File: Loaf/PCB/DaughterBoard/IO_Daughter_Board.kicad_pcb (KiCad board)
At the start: 2 copper layers, 93 x 90.5 mm, 12 parts, among them J1 I/O Block, J2 5V Block, J3 DB25_Socket, J4 Ground Block, J5 Ground Block, J6 Barrel Jack, SW1 SW_Push_Open, SW2 SW_Push_Open

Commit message: Update IO_Daughter_Board.kicad_pcb
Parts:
- SW1: value SW_Push_Open -> ESTOP
- SW2: value SW_Push_Open -> RESET
- moved J2 54.6 mm to (144.5, 67.0), turned to 180 degrees
- moved R2 34.9 mm to (172.6, 79.6)
- moved R3 34.9 mm to (163.1, 79.6)
- moved SW1 34.9 mm to (175.6, 85.8)
- moved SW2 34.9 mm to (159.3, 85.8)
- moved VRM1 14.3 mm to (153.6, 105.6), turned to 180 degrees
- moved J4 2.81 mm to (186.7, 67.0), turned to 180 degrees
- moved J1 0.28 mm to (104.2, 72.7)
- moved J5 0.25 mm to (188.8, 110.8)
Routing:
- net +3.3V: track 0.00 -> 23.8 mm
- net /ESTOP: track 49.6 -> 63.9 mm, vias 0 -> 2
- net /RESET: track 52.3 -> 65.1 mm, vias 0 -> 2
- net +12V: track 21.8 -> 21.1 mm
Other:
- board size 93 x 90.5 mm -> 93 x 55.7 mm

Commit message: Updated Daughter Board
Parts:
- removed R2: 10K, Resistor_THT:R_Axial_DIN0204_L3.6mm_D1.6mm_P7.62mm_Horizontal
- removed SW2: RESET, Button_Switch_THT:SW_PUSH_1P1T_6x3.5mm_H5.0_APEM_MJTP1250
- added J7: Screw_Terminal_01x02, Connector_AMASS:AMASS_XT30UPB-M_1x02_P5.0mm_Vertical, F.Cu at (170.4, 77.7)
- added Logo1: Logo_Open_Hardware_Small, Symbol:OSHW-Symbol_6.7x6mm_SilkScreen, F.Cu at (134.5, 73.8)
- SW1: value ESTOP -> SW_Push; footprint Button_Switch_THT:SW_PUSH_1P1T_6x3.5mm_H5.0_APEM_MJTP1250 -> Button_Switch_THT:SW_Tactile_Straight_KSL0Axx1LFTR
- moved SW1 54.3 mm to (121.3, 86.9)
- moved R3 28.4 mm to (143.4, 100.1)
- moved VRM1 27.6 mm to (179.3, 95.7), turned to -90 degrees
- moved J2 8.74 mm to (174.7, 100.3)
- moved C4 7.63 mm to (137.9, 99.7)
- moved J1 7.47 mm to (156.1, 104.7)
- moved J6 4.08 mm to (184.8, 110.9)
- moved J3 4.01 mm to (108.2, 72.9)
- renumbered J3 to J1, J6 to J2, J1 to J3, J2 to J4, J4 to J5, J5 to J6
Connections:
- C4 pad 1: +5V -> +5V Slice
- J1 pad 20: +5V -> +5V Slice
- J1 pad 7: +5V -> +5V Slice
- J2 pad 1: GND -> +12V
- J2 pad 2: +12V -> GND
- SW1 pad 2: /ESTOP -> /RESET
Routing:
- net +5V: track 0.00 -> 178.9 mm, vias 0 -> 11
- net /RESET: track 65.1 -> 84.2 mm
- net /ESTOP: track 63.9 -> 48.8 mm
- net GND: track 13.5 -> 0.00 mm
- net +5V Slice: track 0.00 -> 8.43 mm
- net /DIO2: track 78.3 -> 71.9 mm
- net /DIO4: track 70.2 -> 64.0 mm
- net /DIO5: track 69.1 -> 62.9 mm
- net /DIO6: track 62.4 -> 56.2 mm
- net /AIO0: track 32.3 -> 26.1 mm
- net /DIO7: track 61.1 -> 55.1 mm
- net /AIO3: track 31.5 -> 25.5 mm
- net /DIO0: track 85.7 -> 79.7 mm
- net /DIO1: track 84.6 -> 78.6 mm
- net /AIO6: track 24.9 -> 30.8 mm
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- added copper zone on F.Cu, net GND
- removed copper zone on F.Cu, net +5V
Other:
- board size 93 x 55.7 mm -> 84.5 x 50.1 mm
- board text added: "Analog I/O"
- board text added: "BREAD I/O Board V1 oshe.io REV 2026"
- board text added: "Digital I/O"
- board text added: "EMERGENCY STOP"
- board text added: "RESET"

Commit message: See Description
Rebuilt I/O Slice daughter board.
Added transmission to the Input slice.
Got digital reading working on input slice.
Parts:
- added H1: MountingHole_Pad, MountingHole:MountingHole_3.2mm_M3_DIN965_Pad, F.Cu at (86.0, 123.0)
- added H2: MountingHole_Pad, MountingHole:MountingHole_3.2mm_M3_DIN965_Pad, F.Cu at (178.0, 123.0)
- added H3: MountingHole_Pad, MountingHole:MountingHole_3.2mm_M3_DIN965_Pad, F.Cu at (93.0, 88.0)
- added H4: MountingHole_Pad, MountingHole:MountingHole_3.2mm_M3_DIN965_Pad, F.Cu at (171.0, 88.0)
- added H5: MountingHole_Pad, MountingHole:MountingHole_3.2mm_M3_DIN965_Pad, F.Cu at (141.5, 103.1)
- added J8: Conn_01x02_Pin, Connector_PinHeader_2.54mm:PinHeader_1x02_P2.54mm_Horizontal, F.Cu at (172.8, 116.5)
- J7: footprint Connector_AMASS:AMASS_XT30UPB-M_1x02_P5.0mm_Vertical -> TerminalBlock:TerminalBlock_MaiXu_MX126-5.0-02P_1x02_P5.00mm
- moved J6 103.9 mm to (85.9, 79.0), turned to -90 degrees
- moved J4 60.4 mm to (178.2, 117.1), turned to 90 degrees
- moved J7 50.4 mm to (147.4, 122.6), turned to 0 degrees
- moved Logo1 35.6 mm to (106.3, 95.5)
- moved C4 29.7 mm to (111.4, 113.0), turned to 90 degrees
- moved SW1 28.5 mm to (114.2, 114.5), turned to 90 degrees
- moved J1 26.9 mm to (133.3, 119.1)
- moved R3 23.1 mm to (120.5, 103.3), turned to 180 degrees
- moved J3 22.8 mm to (129.7, 80.7), turned to 180 degrees
- moved J5 19.7 mm to (172.6, 80.7)
- moved J2 19.3 mm to (161.7, 114.6)
- moved VRM1 18.7 mm to (170.2, 112.0), turned to 180 degrees
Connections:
- J3 pad 10: /AIO1 -> /AIO6
- J3 pad 11: /AIO2 -> /AIO5
- J3 pad 12: /AIO3 -> /AIO4
- J3 pad 13: /AIO4 -> /AIO3
- J3 pad 14: /AIO5 -> /AIO2
- J3 pad 15: /AIO6 -> /AIO1
- J3 pad 16: /AIO7 -> /AIO0
- J3 pad 9: /AIO0 -> /AIO7
- J7 pad 1: +5V -> /ESTOP
- J7 pad 2: /ESTOP -> +5V Slice
- SW1 pad 1: +5V -> +5V Slice
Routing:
- net /RESET: track 84.2 -> 19.6 mm, vias 2 -> 0
- net +5V: track 178.9 -> 114.4 mm, vias 11 -> 5
- net /URX: track 0.00 -> 58.5 mm, vias 0 -> 1
- net +5V Slice: track 8.43 -> 59.6 mm
- net /UTX: track 0.00 -> 50.3 mm, vias 0 -> 1
- net /DIO0: track 79.7 -> 42.0 mm, vias 1 -> 2
- net /DIO1: track 78.6 -> 46.0 mm, vias 1 -> 2
- net /DIO2: track 71.9 -> 44.3 mm, vias 1 -> 2
- net /DIO3: track 70.8 -> 48.6 mm, vias 1 -> 2
- net /AIO3: track 25.5 -> 46.3 mm, vias 1 -> 2
- net /AIO2: track 23.8 -> 43.5 mm, vias 1 -> 2
- net /AIO1: track 27.8 -> 46.5 mm, vias 1 -> 2
- net /AIO0: track 26.1 -> 43.8 mm, vias 1 -> 2
- net /DIO4: track 64.0 -> 46.7 mm, vias 1 -> 2
- net /AIO5: track 26.8 -> 44.0 mm, vias 1 -> 2
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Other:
- board size 84.5 x 50.1 mm -> 100 x 50 mm
- board text added: "BREAD I/O Sub Board V1 oshe.io REV 2026"
- board text added: "E STOP"
- board text added: "UART"
- board text removed: "Analog I/O"
- board text removed: "BREAD I/O Board V1 oshe.io REV 2026"
- board text removed: "Digital I/O"
- board text removed: "EMERGENCY STOP"

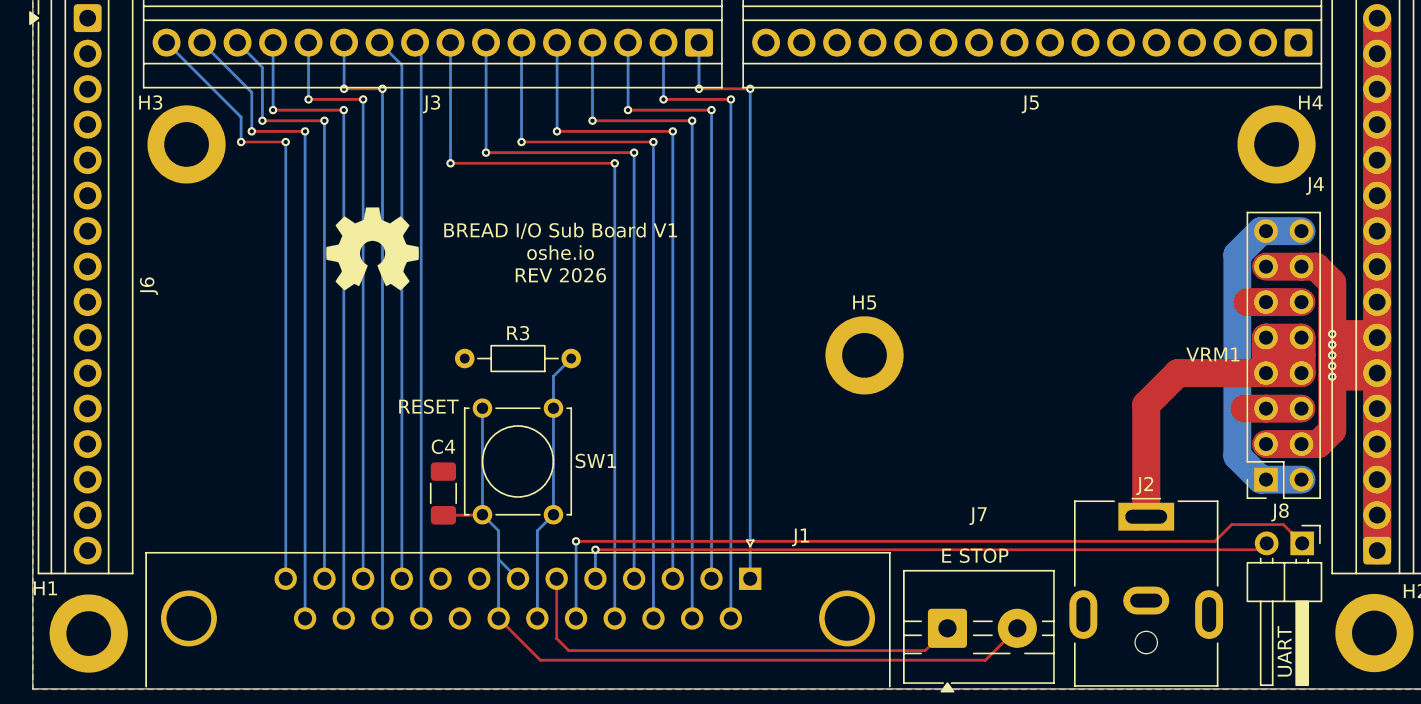
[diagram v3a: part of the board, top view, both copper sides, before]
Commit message: Updated DRC to fit new OSHE specs
pain
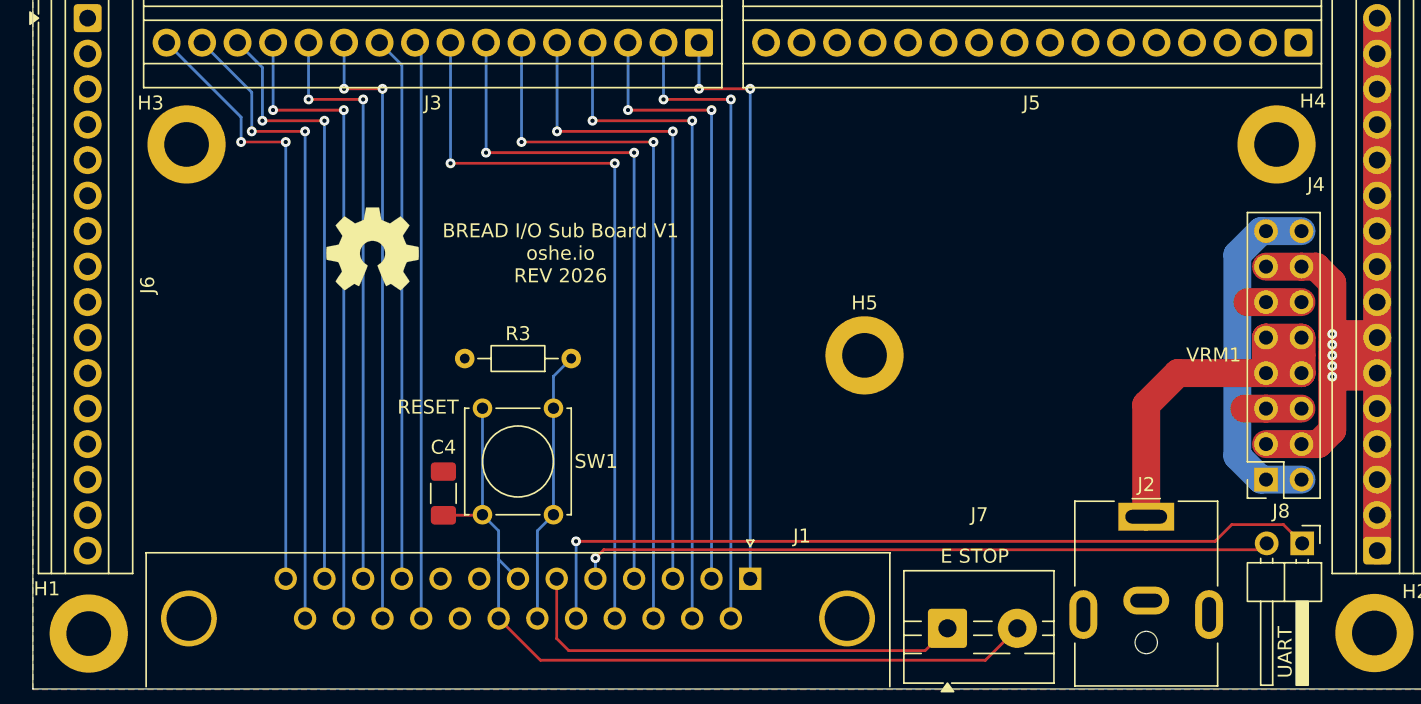
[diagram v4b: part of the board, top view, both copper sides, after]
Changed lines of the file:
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@@
 	)
 	(setup
+		(stackup
+			(layer "F.SilkS"
+				(type "Top Silk Screen")
+			)
+			(layer "F.Paste"
+				(type "Top Solder Paste")
+			)
+			(layer "F.Mask"
+				(type "Top Solder Mask")
+				(thickness 0.01)
+			)
+			(layer "F.Cu"
+				(type "copper")
+				(thickness 0.035)
+			)
+			(layer "dielectric 1"
+				(type "core")
+				(thickness 1.51)
+				(material "FR4")
+				(epsilon_r 4.5)
+				(loss_tangent 0.02)
+			)
+			(layer "B.Cu"
+				(type "copper")
+				(thickness 0.035)
+			)
+			(layer "B.Mask"
+				(type "Bottom Solder Mask")
+				(thickness 0.01)
+			)
+			(layer "B.Paste"
+				(type "Bottom Solder Paste")
+			)
+			(layer "B.SilkS"
+				(type "Bottom Silk Screen")
+			)
+			(copper_finish "None")
+			(dielectric_constraints no)
+		)
 		(pad_to_mask_clearance 0)
 		(allow_soldermask_bridges_in_footprints no)
@@
 		(tags "mountinghole M3 DIN965")
 		(property "Reference" "H1"
-			(at -3.1 -3.2 0)
+			(at -3 -3.2 0)
 			(layer "F.SilkS")
 			(effects
@@
 		(tags "mountinghole M3 DIN965")
 		(property "Reference" "H4"
-			(at 2.424 -2.962 0)
+			(at 2.6 -3.1 0)
 			(layer "F.SilkS")
 			(effects
@@
 	(via
 		(at 129.67 84.016)
-		(size 0.6)
+		(size 0.7064)
 		(drill 0.3)
 		(layers "F.Cu" "B.Cu")
@@
 	(via
 		(at 133.337 84.016)
-		(size 0.6)
+		(size 0.7064)
 		(drill 0.3)
 		(layers "F.Cu" "B.Cu")
@@
 	)
 	(segment
-		(start 133.337 84.016)
-		(end 133.337 119.08)
+		(start 129.67 80.714)
+		(end 129.67 84.016)
 		(width 0.2)
 		(layer "B.Cu")
@@
 	)
 	(segment
-		(start 129.67 80.714)
-		(end 129.67 84.016)
+		(start 133.337 84.016)
+		(end 133.337 119.08)
 		(width 0.2)
 		(layer "B.Cu")
@@
 	)
 	(via
-		(at 131.956 84.778)
-		(size 0.6)
+		(at 131.952 84.778)
+		(size 0.7064)
 		(drill 0.3)
 		(layers "F.Cu" "B.Cu")
@@
 	(via
 		(at 127.13 84.778)
-		(size 0.6)
+		(size 0.7064)
 		(drill 0.3)
 		(layers "F.Cu" "B.Cu")
@@
 	)
 	(segment
-		(start 127.13 80.714)
-		(end 127.13 84.778)
-		(width 0.2)
-		(layer "B.Cu")
-		(net "/DIO1")
-	)
-	(segment
-		(start 131.952 121.92)
-		(end 131.952 84.782)
+		(start 131.952 84.778)
+		(end 131.952 121.92)
 		(width 0.2)
 		(layer "B.Cu")
@@
 	)
 	(segment
-		(start 131.952 84.782)
-		(end 131.956 84.778)
+		(start 127.13 80.714)
+		(end 127.13 84.778)
 		(width 0.2)
 		(layer "B.Cu")
@@
 	(via
 		(at 124.59 85.54)
-		(size 0.6)
+		(size 0.7064)
 		(drill 0.3)
 		(layers "F.Cu" "B.Cu")
@@
 	(via
 		(at 130.567 85.54)
-		(size 0.6)
+		(size 0.7064)
 		(drill 0.3)
 		(layers "F.Cu" "B.Cu")
@@
 	(via
 		(at 122.05 86.302)
-		(size 0.6)
+		(size 0.7064)
 		(drill 0.3)
 		(layers "F.Cu" "B.Cu")
@@
 	(via
 		(at 129.182 86.302)
-		(size 0.6)
+		(size 0.7064)
 		(drill 0.3)
 		(layers "F.Cu" "B.Cu")
@@
 	(via
 		(at 119.51 87.064)
-		(size 0.6)
+		(size 0.7064)
 		(drill 0.3)
 		(layers "F.Cu" "B.Cu")
@@
 	(via
 		(at 127.797 87.064)
-		(size 0.6)
+		(size 0.7064)
 		(drill 0.3)
 		(layers "F.Cu" "B.Cu")
@@
 	(via
 		(at 126.412 87.826)
-		(size 0.6)
+		(size 0.7064)
 		(drill 0.3)
 		(layers "F.Cu" "B.Cu")
@@
 	(via
 		(at 116.97 87.826)
-		(size 0.6)
+		(size 0.7064)
 		(drill 0.3)
 		(layers "F.Cu" "B.Cu")
@@
 	(via
 		(at 114.43 88.588)
-		(size 0.6)
+		(size 0.7064)
 		(drill 0.3)
 		(layers "F.Cu" "B.Cu")
@@
 	(via
 		(at 125.027 88.588)
-		(size 0.6)
+		(size 0.7064)
 		(drill 0.3)
 		(layers "F.Cu" "B.Cu")
@@
 	(via
 		(at 123.642 89.35)
-		(size 0.6)
+		(size 0.7064)
 		(drill 0.3)
 		(layers "F.Cu" "B.Cu")
@@
 	(via
 		(at 111.89 89.35)
-		(size 0.6)
+		(size 0.7064)
 		(drill 0.3)
 		(layers "F.Cu" "B.Cu")
@@
 	(via
 		(at 104.27 84.016)
-		(size 0.6)
+		(size 0.7064)
 		(drill 0.3)
 		(layers "F.Cu" "B.Cu")
@@
 	(via
 		(at 107.022 84.016)
-		(size 0.6)
+		(size 0.7064)
 		(drill 0.3)
 		(layers "F.Cu" "B.Cu")
@@
 	(via
 		(at 101.73 84.778)
-		(size 0.6)
+		(size 0.7064)
 		(drill 0.3)
 		(layers "F.Cu" "B.Cu")
@@
 	(via
 		(at 105.637 84.778)
-		(size 0.6)
+		(size 0.7064)
 		(drill 0.3)
 		(layers "F.Cu" "B.Cu")
@@
 	(via
 		(at 99.19 85.54)
-		(size 0.6)
+		(size 0.7064)
 		(drill 0.3)
 		(layers "F.Cu" "B.Cu")
@@
 	(via
 		(at 104.252 85.54)
-		(size 0.6)
+		(size 0.7064)
 		(drill 0.3)
 		(layers "F.Cu" "B.Cu")
@@
 	(via
 		(at 98.428 86.302)
-		(size 0.6)
+		(size 0.7064)
 		(drill 0.3)
 		(layers "F.Cu" "B.Cu")
@@
 	(via
 		(at 102.867 86.302)
-		(size 0.6)
+		(size 0.7064)
 		(drill 0.3)
 		(layers "F.Cu" "B.Cu")
@@
 	(via
 		(at 101.482 87.064)
-		(size 0.6)
+		(size 0.7064)
 		(drill 0.3)
 		(layers "F.Cu" "B.Cu")
@@
 	(via
 		(at 97.666 87.064)
-		(size 0.6)
+		(size 0.7064)
 		(drill 0.3)
 		(layers "F.Cu" "B.Cu")
@@
 	(via
 		(at 100.097 87.826)
-		(size 0.6)
+		(size 0.7064)
 		(drill 0.3)
 		(layers "F.Cu" "B.Cu")
@@
 	(via
 		(at 96.904 87.826)
-		(size 0.6)
+		(size 0.7064)
 		(drill 0.3)
 		(layers "F.Cu" "B.Cu")
@@
 	(via
 		(at 120.872 116.4)
-		(size 0.6)
+		(size 0.7064)
 		(drill 0.3)
 		(layers "F.Cu" "B.Cu")
@@
 	)
 	(segment
-		(start 169.838 117)
-		(end 122.257 117)
+		(start 122.257 117.602)
+		(end 122.859 117)
 		(width 0.2)
 		(layer "F.Cu")
@@
 	)
 	(segment
-		(start 170.293 116.545)
+		(start 122.859 117)
 		(end 169.838 117)
 		(width 0.2)
@@
 		(net "/UTX")
 	)
+	(segment
+		(start 169.838 117)
+		(end 170.293 116.545)
+		(width 0.2)
+		(layer "F.Cu")
+		(net "/UTX")
+	)
 	(via
-		(at 122.257 117)
-		(size 0.6)
+		(at 122.257 117.602)
+		(size 0.7064)
 		(drill 0.3)
 		(layers "F.Cu" "B.Cu")
@@
 	)
 	(segment
-		(start 122.257 117)
+		(start 122.257 117.602)
 		(end 122.257 119.08)
 		(width 0.2)
@@
 	(via
 		(at 174.985 102.33)
-		(size 0.6)
+		(size 0.7064)
 		(drill 0.3)
 		(layers "F.Cu" "B.Cu")
@@
 	(via
 		(at 174.985 103.092)
-		(size 0.6)
+		(size 0.7064)
 		(drill 0.3)
 		(layers "F.Cu" "B.Cu")
@@
 	(via
 		(at 174.985 103.854)
-		(size 0.6)
+		(size 0.7064)
 		(drill 0.3)
 		(layers "F.Cu" "B.Cu")
@@
 	(via
 		(at 174.985 101.568)
-		(size 0.6)
+		(size 0.7064)
 		(drill 0.3)
 		(layers "F.Cu" "B.Cu")
@@
 	(via
 		(at 174.985 104.616)
-		(size 0.6)
+		(size 0.7064)
 		(drill 0.3)
 		(layers "F.Cu" "B.Cu")

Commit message: Added OSHE branding to VRM
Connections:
- J1 pad 18: /URX -> /UTX
- J1 pad 5: /UTX -> /URX
- J8 pad 1: /URX -> /UTX
- J8 pad 2: /UTX -> /URX
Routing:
- net /UTX: track 50.0 -> 58.5 mm
- net /URX: track 58.5 -> 50.0 mm
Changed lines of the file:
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@@
 			(layers "*.Cu" "*.Mask")
 			(remove_unused_layers no)
-			(net "/URX")
+			(net "/UTX")
 			(pinfunction "Pin_1_1")
 			(pintype "passive")
@@
 			(layers "*.Cu" "*.Mask")
 			(remove_unused_layers no)
-			(net "/UTX")
+			(net "/URX")
 			(pinfunction "Pin_2_2")
 			(pintype "passive")
@@
 			(layers "*.Cu" "*.Mask")
 			(remove_unused_layers no)
-			(net "/UTX")
+			(net "/URX")
 			(pinfunction "5_5")
 			(pintype "passive")
@@
 			(layers "*.Cu" "*.Mask")
 			(remove_unused_layers no)
-			(net "/URX")
+			(net "/UTX")
 			(pinfunction "P18_18")
 			(pintype "passive")
@@
 	)
 	(segment
-		(start 120.872 116.4)
-		(end 166.6 116.4)
-		(width 0.2)
-		(layer "F.Cu")
-		(net "/URX")
-	)
-	(segment
-		(start 166.6 116.4)
-		(end 167.8 115.2)
+		(start 122.257 117.602)
+		(end 122.859 117)
 		(width 0.2)
 		(layer "F.Cu")
@@
 	)
 	(segment
-		(start 171.488 115.2)
-		(end 172.833 116.545)
+		(start 122.859 117)
+		(end 169.838 117)
 		(width 0.2)
 		(layer "F.Cu")
@@
 	)
 	(segment
-		(start 167.8 115.2)
-		(end 171.488 115.2)
+		(start 169.838 117)
+		(end 170.293 116.545)
 		(width 0.2)
 		(layer "F.Cu")
@@
 	)
 	(via
-		(at 120.872 116.4)
+		(at 122.257 117.602)
 		(size 0.7064)
 		(drill 0.3)
@@
 	)
 	(segment
-		(start 120.872 121.92)
-		(end 120.872 116.4)
+		(start 122.257 117.602)
+		(end 122.257 119.08)
 		(width 0.2)
 		(layer "B.Cu")
@@
 	)
 	(segment
-		(start 122.257 117.602)
-		(end 122.859 117)
+		(start 120.872 116.4)
+		(end 166.6 116.4)
 		(width 0.2)
 		(layer "F.Cu")
@@
 	)
 	(segment
-		(start 122.859 117)
-		(end 169.838 117)
+		(start 166.6 116.4)
+		(end 167.8 115.2)
 		(width 0.2)
 		(layer "F.Cu")
@@
 	)
 	(segment
-		(start 169.838 117)
-		(end 170.293 116.545)
+		(start 171.488 115.2)
+		(end 172.833 116.545)
+		(width 0.2)
+		(layer "F.Cu")
+		(net "/UTX")
+	)
+	(segment
+		(start 167.8 115.2)
+		(end 171.488 115.2)
 		(width 0.2)
 		(layer "F.Cu")
@@
 	)
 	(via
-		(at 122.257 117.602)
+		(at 120.872 116.4)
 		(size 0.7064)
 		(drill 0.3)
@@
 	)
 	(segment
-		(start 122.257 117.602)
-		(end 122.257 119.08)
+		(start 120.872 121.92)
+		(end 120.872 116.4)
 		(width 0.2)
 		(layer "B.Cu")
